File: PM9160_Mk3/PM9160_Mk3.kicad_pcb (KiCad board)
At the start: 2 copper layers, 100 x 40 mm, 87 parts, among them J1 Conn_Coaxial, U1 BGA2869, U2 ATtiny416-M, U3 SY100EL33L, U4 SY100EL33L, U5 LM317L_TO92

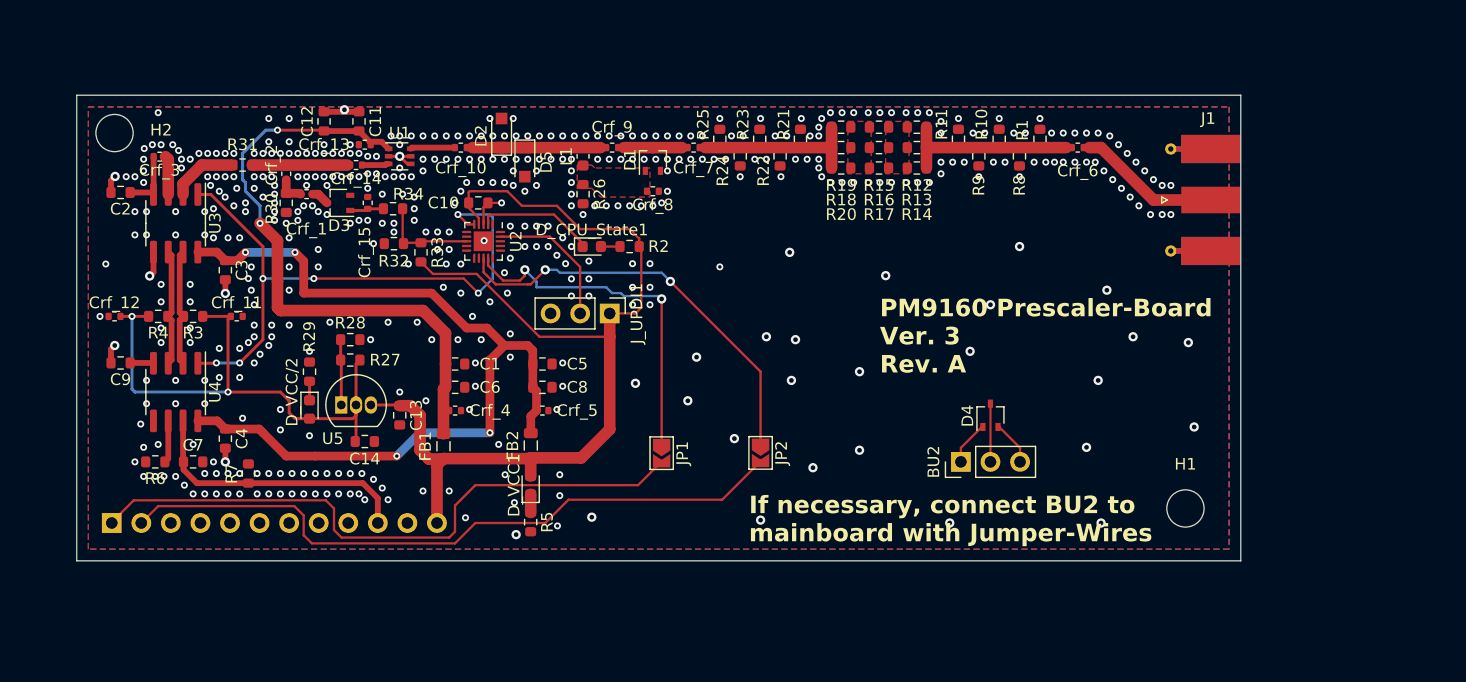
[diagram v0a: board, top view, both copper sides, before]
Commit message: Minor Changes to PCB layout, cleaned up schematic, fixed some DRC/ERC errors and warnings, made board compatible with Aislers "simple" PCB Service
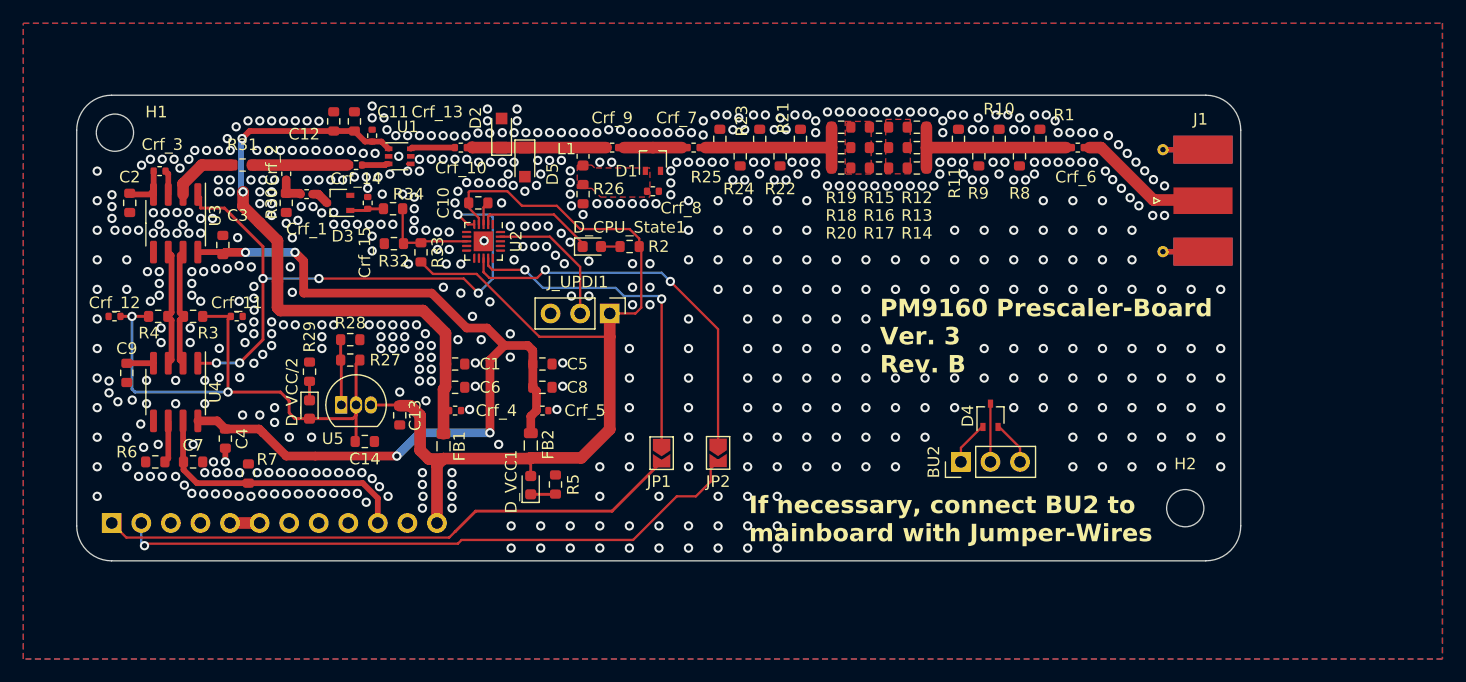
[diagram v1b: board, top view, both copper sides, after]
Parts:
- C1, C12, C5: value 22uF 6.3V -> 22uF
- H1, H2: value MountingHole_Pad -> MountingHole
- moved H1 97.5 mm to (113.3, 93.2)
- moved H2 97.5 mm to (205.2, 125.5)
- moved R5 3.87 mm to (151.1, 123.4), turned to 90 degrees
- moved JP2 3.65 mm to (165.1, 120.7)
- moved C3 2.17 mm to (122.6, 102.9), turned to 90 degrees
- moved Crf_3 1.24 mm to (117.1, 96.5)
- moved C2 1.19 mm to (114.6, 99.2), turned to -90 degrees
- moved C9 1.01 mm to (114.3, 113.9), turned to -90 degrees
- moved Crf_13 1.00 mm to (135.4, 93.5), turned to -90 degrees
- moved C12 0.83 mm to (132.1, 92.2)
- moved J1 0.68 mm to (205.0, 99.1)
- moved C11 0.39 mm to (133.9, 92.2)
- turned R30 to -90 degrees
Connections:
- net CPU_STATE renamed Net-(D_CPU_State1-K)
- net Net-(Crf_10-Pad2) renamed Input_atten
- R30 pad 1: GND -> Net-(Crf_1-Pad2)
- R30 pad 2: Net-(Crf_1-Pad2) -> GND
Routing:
- net GND: track 17.3 -> 3.68 mm, vias 462 -> 634
- net !B: track 54.5 -> 50.5 mm
- net TEST_GO: track 59.0 -> 55.1 mm, vias 0 -> 1
- net Net-(BU7-Pin_5): track 0.00 -> 2.54 mm
- net Net-(JP2-A): track 35.8 -> 33.9 mm
- net Net-(JP1-A): track 30.6 -> 29.2 mm
- net Net-(U3-!CLK): track 3.34 -> 2.10 mm
- net +5VA: track 52.6 -> 53.6 mm
- net Net-(U3-VBB): track 5.32 -> 4.33 mm
- net Net-(D_VCC1-K): track 1.56 -> 2.14 mm
- net Net-(D2-K): track 11.0 -> 11.6 mm
- net RF_RESET: track 52.8 -> 53.3 mm
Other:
- outline, holes or cut-outs redrawn
- board text added: "PM9160 Prescaler-Board Ver. 3 Rev. B"
- board text removed: "PM9160 Prescaler-Board Ver. 3 Rev. A"

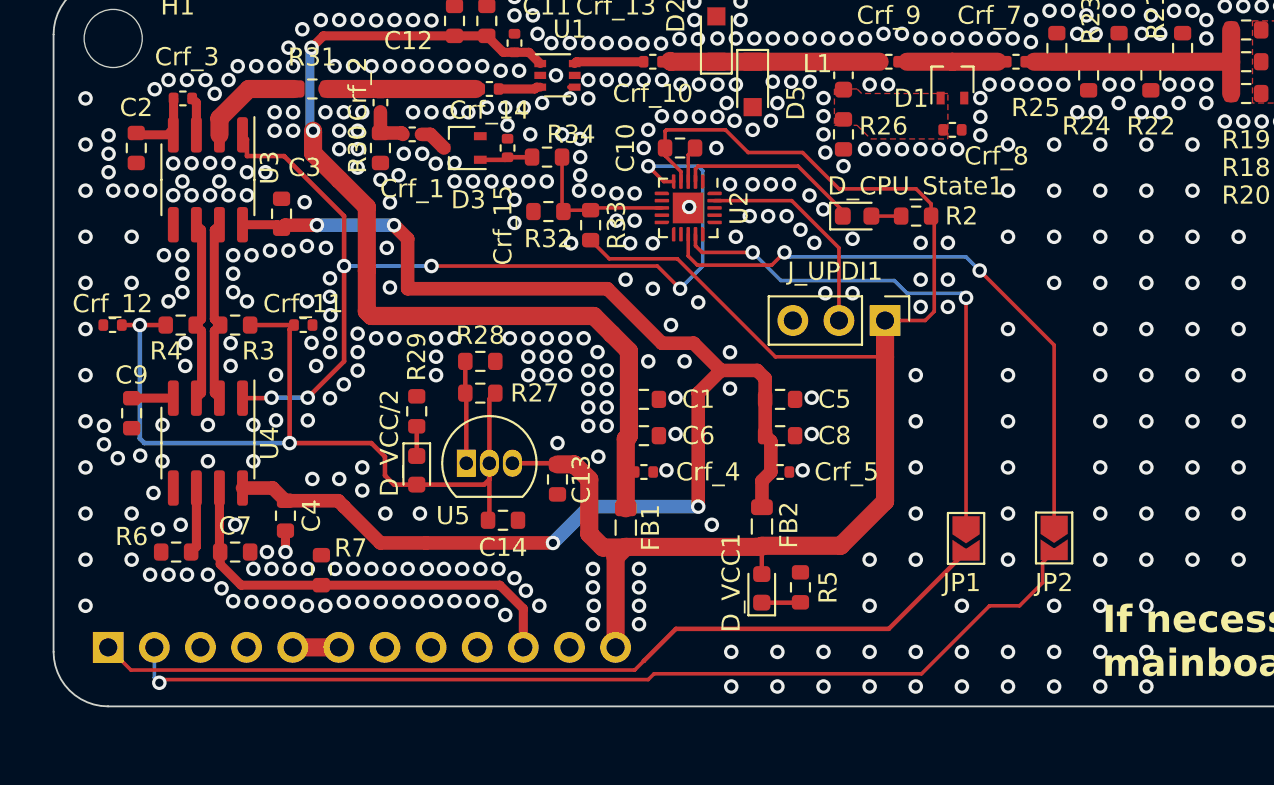
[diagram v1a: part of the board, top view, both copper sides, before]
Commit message: changed microcontroller to SOIC-8 Attiny412 for easier handsoldering.
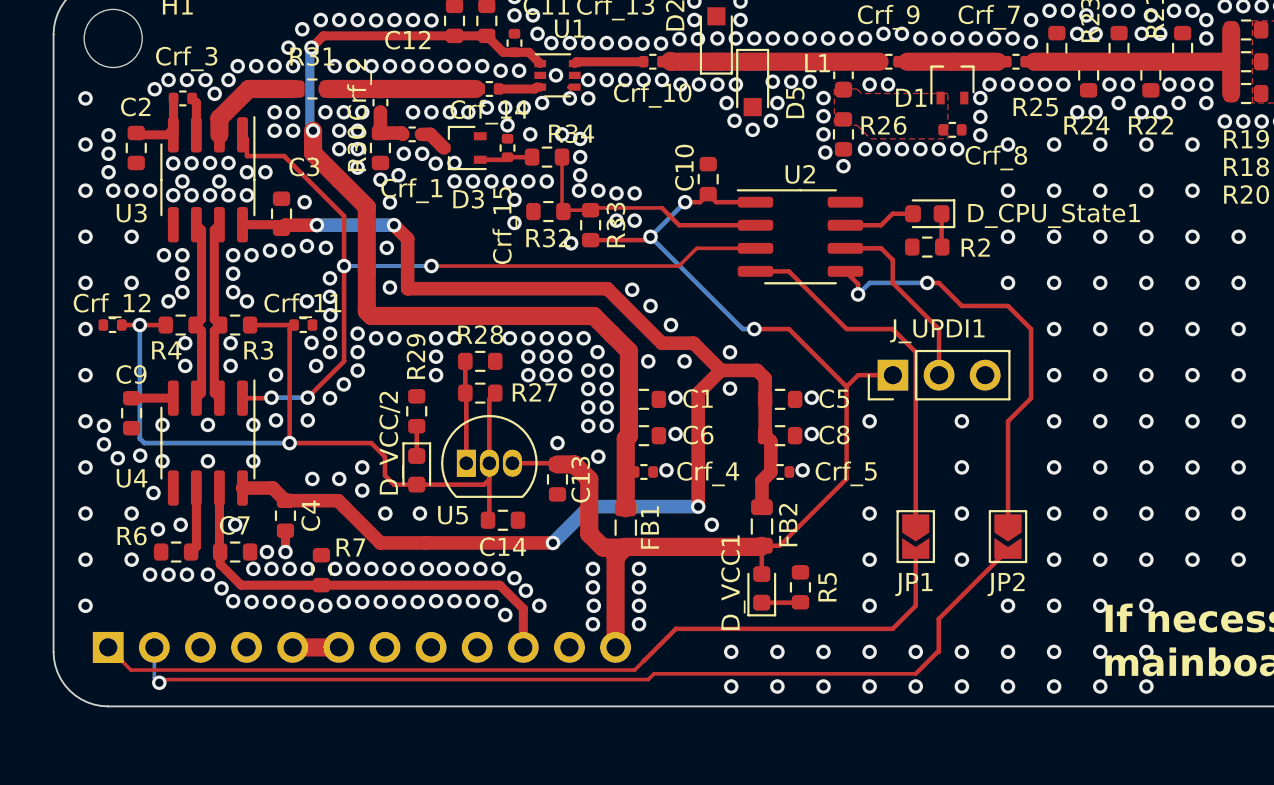
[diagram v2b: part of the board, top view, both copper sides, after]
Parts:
- U2: value ATtiny416-M -> ATtiny412-SS; footprint Package_DFN_QFN:VQFN-20-1EP_3x3mm_P0.4mm_EP1.7x1.7mm -> Package_SO:SOIC-8_3.9x4.9mm_P1.27mm
- moved U2 6.38 mm to (151.1, 104.1), turned to 0 degrees
- moved D_CPU_State1 3.87 mm to (158.1, 102.9), turned to 180 degrees
- moved J_UPDI1 3.04 mm to (156.2, 111.8), turned to 90 degrees
- moved JP1 2.77 mm to (157.5, 120.7)
- moved JP2 2.54 mm to (162.6, 120.7)
- moved C10 2.31 mm to (146.1, 101.0), turned to -90 degrees
- moved R2 1.81 mm to (158.1, 104.7), turned to 180 degrees
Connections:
- R2 pad 1: Net-(D_CPU_State1-A) -> Net-(D_CPU_State1-K)
- R2 pad 2: +5V -> GND
- U2 pad 1: unconnected-(U2-PA2-Pad1) -> +5V
- U2 pad 2: Net-(D_CPU_State1-K) -> RF_DETECT
- U2 pad 3: GND -> RF_RESET
- U2 pad 4: +5V -> Net-(JP1-A)
- U2 pad 5: RF_RESET -> Net-(JP2-A)
- U2 pad 6: unconnected-(U2-PA5-Pad6) -> UPDI
- U2 pad 7: unconnected-(U2-PA6-Pad7) -> Net-(D_CPU_State1-A)
- U2 pad 8: RF_DETECT -> GND
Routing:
- net +5V: track 89.8 -> 63.4 mm, vias 0 -> 3
- net Net-(JP2-A): track 33.9 -> 23.6 mm
- net Net-(JP1-A): track 29.2 -> 20.1 mm, vias 2 -> 0
- net Net-(D_CPU_State1-K): track 10.2 -> 1.85 mm
- net RF_RESET: track 53.3 -> 45.5 mm, vias 6 -> 4
- net RF_DETECT: track 8.54 -> 14.1 mm
- net Net-(D_CPU_State1-A): track 1.64 -> 3.99 mm
- net TEST_GO: track 55.1 -> 53.0 mm
- net GND: track 3.68 -> 1.67 mm, vias 634 -> 604
- net UPDI: track 11.9 -> 10.3 mm
- net !B: track 50.5 -> 49.5 mm

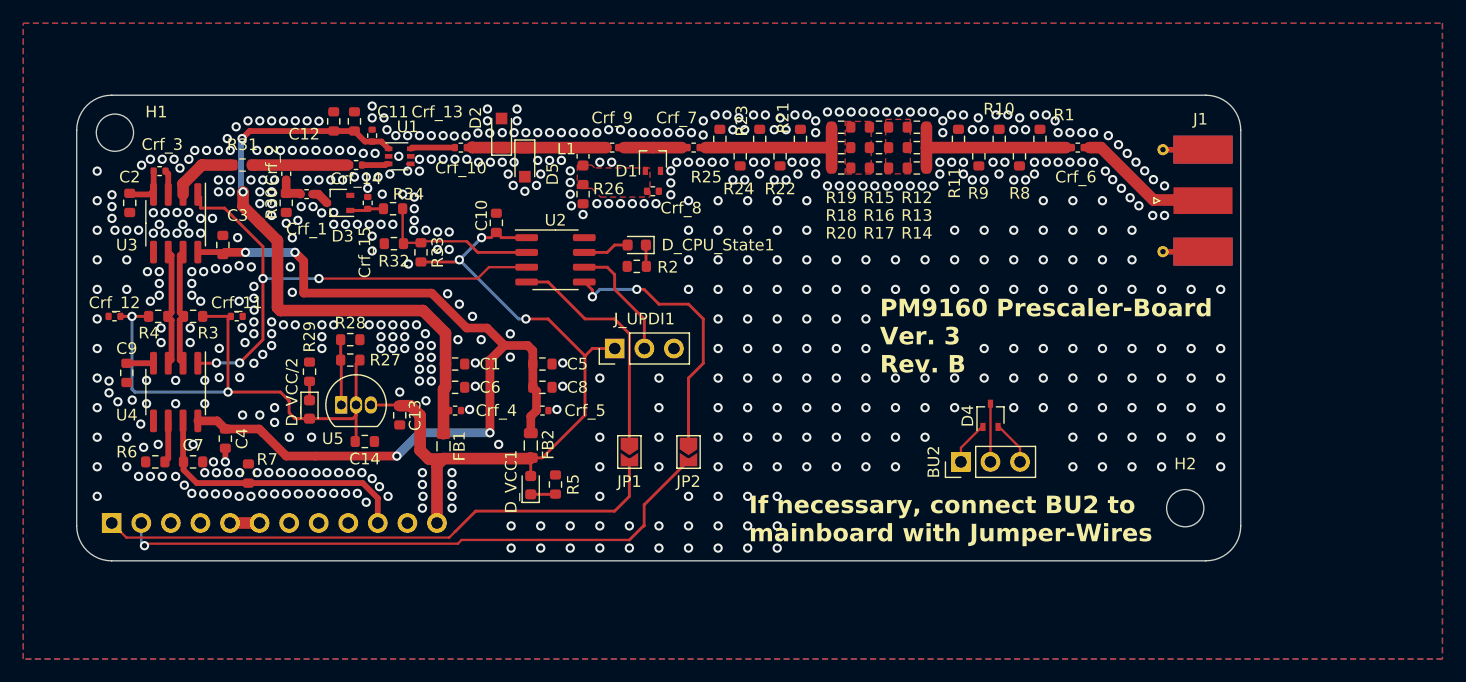
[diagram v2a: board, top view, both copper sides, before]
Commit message: Changed resistor-footprints of the capacitors to proper capacitor footprints.
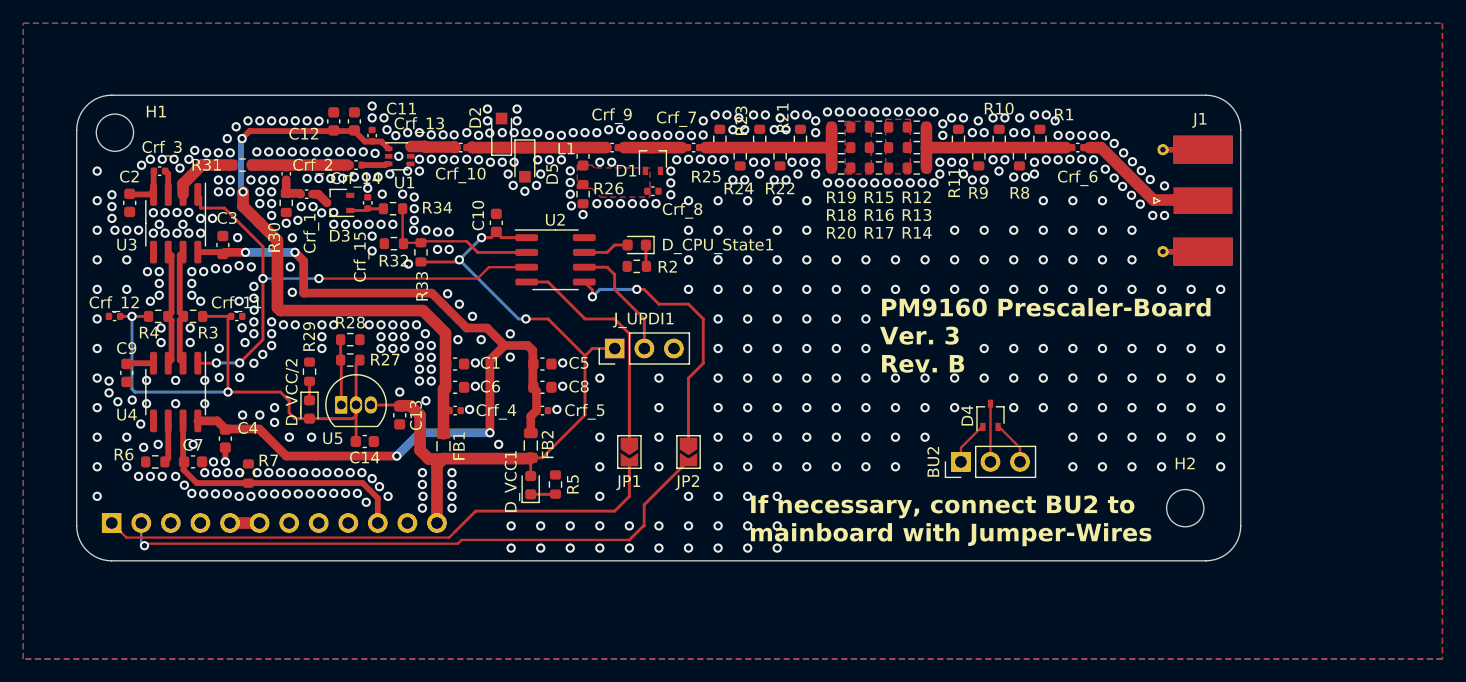
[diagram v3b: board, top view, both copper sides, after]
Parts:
- C1, C10, C11, C12, C13, C14, C2, C3, C4, C5, C6, C7, C8, C9: footprint Resistor_SMD:R_0603_1608Metric -> Capacitor_SMD:C_0603_1608Metric
- Crf_1, Crf_10, Crf_11, Crf_12, Crf_13, Crf_14, Crf_15, Crf_2, Crf_3, Crf_4, Crf_5, Crf_6, Crf_7, Crf_8, Crf_9: footprint Resistor_SMD:R_0402_1005Metric -> Capacitor_SMD:C_0402_1005Metric
